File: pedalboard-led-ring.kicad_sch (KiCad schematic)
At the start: 16 parts, among them J1 Conn_02x03, U1 TLC5973, U2 LT3494AEDDBPBF

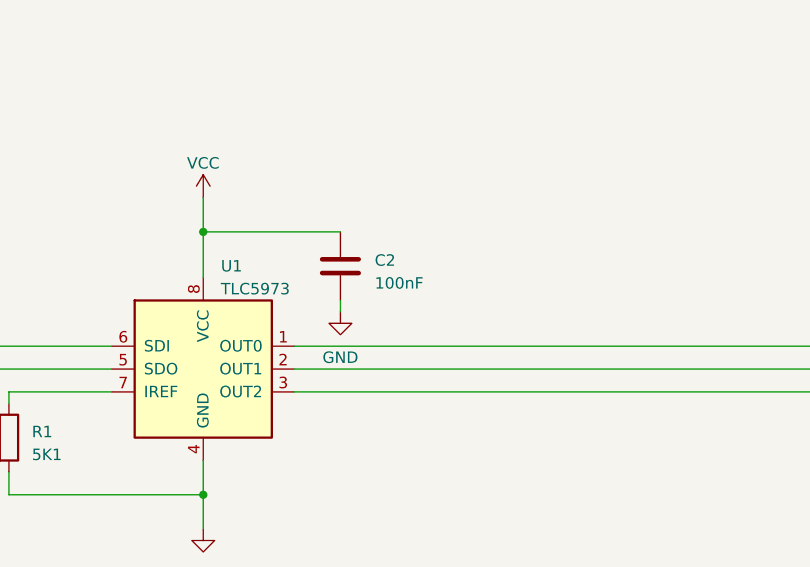
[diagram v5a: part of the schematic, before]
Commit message: Start to collect datasheets and parts on digikey
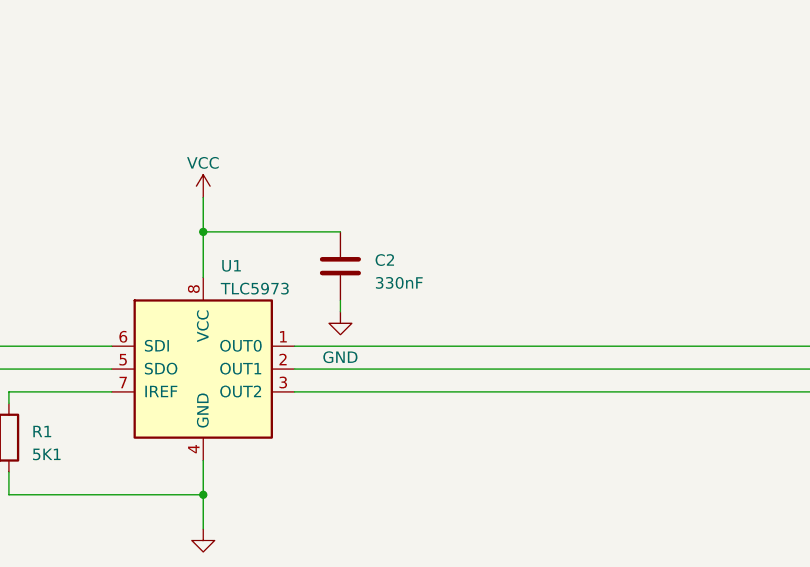
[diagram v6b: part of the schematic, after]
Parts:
- C1, C3, L1: SUPPLIER (none) -> https://www.digikey.ch/de/products/detail/murata-electronic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
- C2: value 100nF -> 330nF; SUPPLIER (none) -> https://www.digikey.ch/de/products/detail/murata-electronic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
- C4: value 0.22uF_0603_25V -> 330nF; SUPPLIER (none) -> https://www.digikey.ch/de/products/detail/murata-electronic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
- D1, D2, D3, D4, D5, D6: SUPPLIER (none) -> https://www.digikey.ch/de/products/detail/harvatek-corporat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
- J1: SUPPLIER (none) -> https://www.digikey.ch/de/products/detail/preci-dip/853-87-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
- R1, R2: SUPPLIER (none) -> https://www.digikey.ch/de/products/detail/samsung-electro-m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
- U1: SUPPLIER (none) -> https://www.digikey.ch/en/products/detail/texas-instruments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
- U2: SUPPLIER Linear Technology -> https://www.digikey.ch/de/products/detail/analog-devices-in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
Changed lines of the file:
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@@
       (effects (font (size 1.27 1.27)) hide)
     )
-    (property "Datasheet" "" (at 210.82 38.1 0)
+    (property "Datasheet" "https://search.murata.co.jp/Ceramy/image/img/A01X/G101/ENG/GRT31CR61H225KE01-01.pdf" (at 210.82 38.1 0)
       (effects (font (size 1.27 1.27)) hide)
     )
@@
       (effects (font (size 1.27 1.27)) hide)
     )
+    (property "SUPPLIER" "https://www.digikey.ch/de/products/detail/murata-electronics/GRT31CR61H225KE01L/5416882" (at 210.82 38.1 0)
+      (effects (font (size 1.27 1.27)) hide)
+    )
     (pin "1")
     (pin "2")
@@
       (effects (font (size 1.27 1.27)) (justify left) hide)
     )
-    (property "Datasheet" "https://search.murata.co.jp/Ceramy/image/img/A01X/G101/ENG/GRM21BR61E106MA73-01.pdf" (at 39.37 40.64 0)
+    (property "Datasheet" "https://search.murata.co.jp/Ceramy/image/img/A01X/G101/ENG/GRT31CR6YA106KE01-01.pdf" (at 39.37 40.64 0)
       (effects (font (size 1.27 1.27)) hide)
     )
@@
       (effects (font (size 1.27 1.27)) hide)
     )
+    (property "SUPPLIER" "https://www.digikey.ch/de/products/detail/murata-electronics/GRT31CR6YA106KE01K/13904946" (at 39.37 40.64 0)
+      (effects (font (size 1.27 1.27)) hide)
+    )
     (pin "1")
     (pin "2")
@@
       (effects (font (size 1.27 1.27)) (justify left) hide)
     )
+    (property "SUPPLIER" "https://www.digikey.ch/de/products/detail/harvatek-corporation/B3803FCH-20C001112U1930/13588742" (at 191.77 77.47 0)
+      (effects (font (size 1.27 1.27)) hide)
+    )
     (pin "1")
     (pin "2")
@@
     (property "Datasheet" "https://media.digikey.com/pdf/Data%20Sheets/Harvatek%20PDFs/B3803FCH-20C001112U1930%20V1.3.pdf" (at 191.77 127 0)
       (effects (font (size 1.27 1.27)) (justify left) hide)
+    )
+    (property "SUPPLIER" "https://www.digikey.ch/de/products/detail/harvatek-corporation/B3803FCH-20C001112U1930/13588742" (at 191.77 123.19 0)
+      (effects (font (size 1.27 1.27)) hide)
     )
     (pin "1")
@@
       (effects (font (size 1.27 1.27)) hide)
     )
+    (property "SUPPLIER" "https://www.digikey.ch/de/products/detail/murata-electronics/LQH32CN150K53L/1016219" (at 57.15 43.18 0)
+      (effects (font (size 1.27 1.27)) hide)
+    )
     (pin "1")
     (pin "2")
@@
       (effects (font (size 1.27 1.27)) hide)
     )
-    (property "Datasheet" "~" (at 91.44 143.51 0)
+    (property "Datasheet" "https://media.digikey.com/pdf/Data%20Sheets/Samsung%20PDFs/RC_Series_ds.pdf" (at 91.44 143.51 0)
+      (effects (font (size 1.27 1.27)) hide)
+    )
+    (property "SUPPLIER" "https://www.digikey.ch/de/products/detail/samsung-electro-mechanics/RC1608F512CS/3965020" (at 91.44 143.51 0)
       (effects (font (size 1.27 1.27)) hide)
     )
@@
       (effects (font (size 1.27 1.27)) (justify left))
     )
-    (property "Value" "0.22uF_0603_25V" (at 52.07 50.8 0)
+    (property "Value" "330nF" (at 52.07 50.8 0)
       (effects (font (size 1.27 1.27)) hide)
     )
@@
       (effects (font (size 1.27 1.27)) (justify left) hide)
     )
-    (property "Datasheet" "" (at 52.07 54.61 0)
+    (property "Datasheet" "https://search.murata.co.jp/Ceramy/image/img/A01X/G101/ENG/GRM216R61A334KA01-01.pdf" (at 52.07 54.61 0)
       (effects (font (size 1.27 1.27)) hide)
     )
@@
       (effects (font (size 1.27 1.27)) (justify left))
     )
+    (property "SUPPLIER" "https://www.digikey.ch/de/products/detail/murata-electronics/GRM216R61A334KA01D/2545090" (at 52.07 54.61 0)
+      (effects (font (size 1.27 1.27)) hide)
+    )
     (pin "1")
     (pin "2")
@@
       (effects (font (size 1.27 1.27)) (justify left) hide)
     )
+    (property "SUPPLIER" "https://www.digikey.ch/de/products/detail/harvatek-corporation/B3803FCH-20C001112U1930/13588742" (at 191.77 92.71 0)
+      (effects (font (size 1.27 1.27)) hide)
+    )
     (pin "1")
     (pin "2")
@@
     (property "Datasheet" "https://media.digikey.com/pdf/Data%20Sheets/Harvatek%20PDFs/B3803FCH-20C001112U1930%20V1.3.pdf" (at 191.77 111.76 0)
       (effects (font (size 1.27 1.27)) (justify left) hide)
+    )
+    (property "SUPPLIER" "https://www.digikey.ch/de/products/detail/harvatek-corporation/B3803FCH-20C001112U1930/13588742" (at 191.77 107.95 0)
+      (effects (font (size 1.27 1.27)) hide)
     )
     (pin "1")
@@
       (effects (font (size 1.27 1.27)) (justify left))
     )
-    (property "Value" "100nF" (at 132.08 126.365 0)
+    (property "Value" "330nF" (at 132.08 126.365 0)
       (effects (font (size 1.27 1.27)) (justify left))
     )
@@
       (effects (font (size 1.27 1.27)) hide)
     )
-    (property "Datasheet" "~" (at 128.27 124.46 0)
+    (property "Datasheet" "https://search.murata.co.jp/Ceramy/image/img/A01X/G101/ENG/GRM216R61A334KA01-01.pdf" (at 128.27 124.46 0)
+      (effects (font (size 1.27 1.27)) hide)
+    )
+    (property "SUPPLIER" "https://www.digikey.ch/de/products/detail/murata-electronics/GRM216R61A334KA01D/2545090" (at 128.27 124.46 0)
       (effects (font (size 1.27 1.27)) hide)
     )
@@
       (effects (font (size 1.27 1.27)) (justify left) hide)
     )
+    (property "SUPPLIER" "https://www.digikey.ch/de/products/detail/harvatek-corporation/B3803FCH-20C001112U1930/13588742" (at 191.77 46.99 0)
+      (effects (font (size 1.27 1.27)) hide)
+    )
     (pin "1")
     (pin "2")
@@
       (effects (font (size 1.27 1.27)) (justify left) hide)
     )
-    (property "Datasheet" "http://www.ti.com/lit/ds/symlink/tlc5973.pdf" (at 105.41 127 0)
+    (property "Datasheet" "https://www.ti.com/lit/ds/symlink/tlc5973.pdf" (at 105.41 127 0)
+      (effects (font (size 1.27 1.27)) hide)
+    )
+    (property "SUPPLIER" "https://www.digikey.ch/en/products/detail/texas-instruments/TLC5973DR/4251271" (at 113.03 135.89 0)
       (effects (font (size 1.27 1.27)) hide)
     )
@@
       (effects (font (size 1.27 1.27)) hide)
     )
-    (property "Datasheet" "~" (at 60.96 30.48 0)
+    (property "Datasheet" "https://media.digikey.com/pdf/Data%20Sheets/Samsung%20PDFs/RC_Series_ds.pdf" (at 60.96 30.48 0)
+      (effects (font (size 1.27 1.27)) hide)
+    )
+    (property "SUPPLIER" "https://www.digikey.ch/de/products/detail/samsung-electro-mechanics/RC1608F3484CS/3965270" (at 60.96 30.48 0)
       (effects (font (size 1.27 1.27)) hide)
     )
@@
       (effects (font (size 1.27 1.27)) (justify left) hide)
     )
+    (property "SUPPLIER" "https://www.digikey.ch/de/products/detail/harvatek-corporation/B3803FCH-20C001112U1930/13588742" (at 191.77 62.23 0)
+      (effects (font (size 1.27 1.27)) hide)
+    )
     (pin "1")
     (pin "2")
@@
       (effects (font (size 1.27 1.27)) hide)
     )
-    (property "Datasheet" "~" (at 54.61 138.43 0)
+    (property "Datasheet" "https://www.precidip.com/AppHost/9696,1/Scripts/Modules/Catalog/Default.aspx?c=7&i=349&p=124&pdf=1&dsku=853-PP-NNN-30-001101" (at 54.61 138.43 0)
+      (effects (font (size 1.27 1.27)) hide)
+    )
+    (property "SUPPLIER" "https://www.digikey.ch/de/products/detail/preci-dip/853-87-006-30-001101/4137372" (at 54.61 138.43 0)
       (effects (font (size 1.27 1.27)) hide)
     )
@@
       (effects (font (size 1.27 1.27)) (justify bottom) hide)
     )
-    (property "Datasheet" "" (at 87.63 44.45 0)
+    (property "Datasheet" "https://www.analog.com/media/en/technical-documentation/data-sheets/3494fb.pdf" (at 87.63 44.45 0)
       (effects (font (size 1.27 1.27)) hide)
     )
@@
       (effects (font (size 1.27 1.27)) (justify bottom) hide)
     )
-    (property "SUPPLIER" "Linear Technology" (at 87.63 44.45 0)
+    (property "SUPPLIER" "https://www.digikey.ch/de/products/detail/analog-devices-inc/LT3494AEDDB-TRPBF/1767840" (at 87.63 44.45 0)
       (effects (font (size 1.27 1.27)) (justify bottom) hide)
     )

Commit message: Fix connector
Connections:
- net GND: now also J1.3 (VCC); no longer J1.4 (VCC)
- net VCC: now also J1.5 (GND); no longer J1.6 (GND)
- net VDC: now also J1.1 (SDO); no longer J1.2 (SDO)
- net at C3.1, L1.2, U2.3 (VCC)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: now also J1.2 (SDI); no longer J1.1 (SDI)
- net at U1.5 (SDO): now also J1.4 (VLED); no longer J1.3 (VLED)
- net at U1.6 (SDI): now also J1.6 (GND); no longer J1.5 (GND)
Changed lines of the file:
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@@
       (effects (font (size 1.27 1.27)) hide)
     )
-    (property "Datasheet" "https://www.precidip.com/AppHost/9696,1/Scripts/Modules/Catalog/Default.aspx?c=7&i=349&p=124&pdf=1&dsku=853-PP-NNN-30-001101" (at 54.61 138.43 0)
+    (property "Datasheet" "~" (at 54.61 138.43 0)
       (effects (font (size 1.27 1.27)) hide)
     )

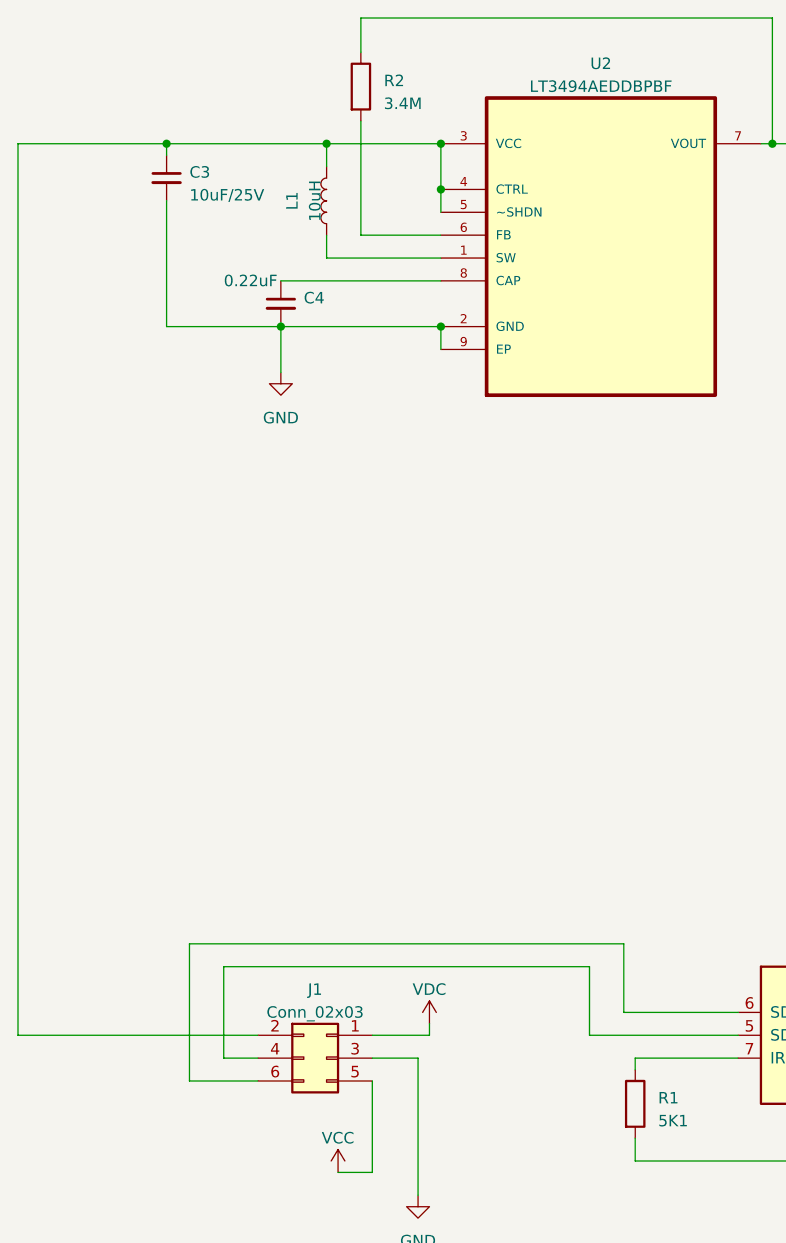
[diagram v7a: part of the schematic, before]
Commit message: Improve copper ground layers
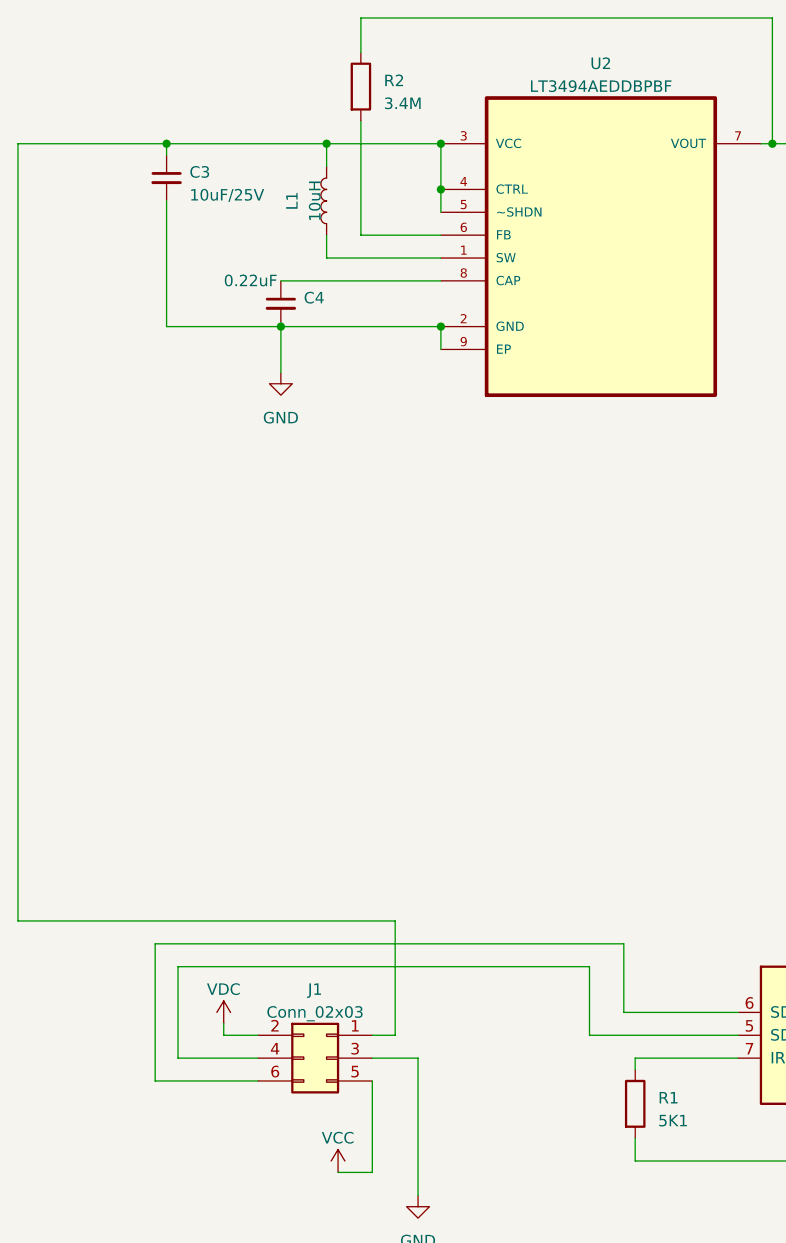
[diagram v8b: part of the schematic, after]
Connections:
- net VDC: now also J1.2 (SDI); no longer J1.1 (SDO)
- net at C3.1, L1.2, U2.3 (VCC)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: now also J1.1 (SDO); no longer J1.2 (SDI)
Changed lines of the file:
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@@
+    (stroke (width 0) (type default))
+  )
+  (wire (pts (xy 22.86 123.19) (xy 64.77 123.19))
     (stroke (width 0) (type default))
   )
@@
     (stroke (width 0) (type default))
   )
-  (wire (pts (xy 49.53 135.89) (xy 22.86 135.89))
-    (stroke (width 0) (type default))
-  )
   (wire (pts (xy 194.31 138.43) (xy 194.31 130.81))
     (stroke (width 0) (type default))
@@
     (stroke (width 0) (type default))
   )
-  (wire (pts (xy 62.23 135.89) (xy 68.58 135.89))
-    (stroke (width 0) (type default))
-  )
-  (wire (pts (xy 41.91 125.73) (xy 41.91 140.97))
+  (wire (pts (xy 64.77 135.89) (xy 62.23 135.89))
+    (stroke (width 0) (type default))
+  )
+  (wire (pts (xy 38.1 125.73) (xy 38.1 140.97))
     (stroke (width 0) (type default))
   )
@@
     (stroke (width 0) (type default))
   )
-  (wire (pts (xy 41.91 140.97) (xy 49.53 140.97))
-    (stroke (width 0) (type default))
-  )
-  (wire (pts (xy 68.58 135.89) (xy 68.58 134.62))
+  (wire (pts (xy 38.1 140.97) (xy 49.53 140.97))
     (stroke (width 0) (type default))
   )
@@
     (stroke (width 0) (type default))
   )
-  (wire (pts (xy 45.72 128.27) (xy 45.72 138.43))
+  (wire (pts (xy 40.64 128.27) (xy 40.64 138.43))
     (stroke (width 0) (type default))
   )
@@
     (stroke (width 0) (type default))
   )
+  (wire (pts (xy 64.77 123.19) (xy 64.77 135.89))
+    (stroke (width 0) (type default))
+  )
   (wire (pts (xy 194.31 35.56) (xy 210.82 35.56))
     (stroke (width 0) (type default))
@@
     (stroke (width 0) (type default))
   )
+  (wire (pts (xy 49.53 135.89) (xy 45.72 135.89))
+    (stroke (width 0) (type default))
+  )
   (wire (pts (xy 113.03 149.86) (xy 113.03 153.67))
     (stroke (width 0) (type default))
@@
     (stroke (width 0) (type default))
   )
-  (wire (pts (xy 90.17 125.73) (xy 41.91 125.73))
+  (wire (pts (xy 90.17 125.73) (xy 38.1 125.73))
+    (stroke (width 0) (type default))
+  )
+  (wire (pts (xy 45.72 135.89) (xy 45.72 134.62))
     (stroke (width 0) (type default))
   )
@@
     (stroke (width 0) (type default))
   )
-  (wire (pts (xy 22.86 36.83) (xy 22.86 135.89))
+  (wire (pts (xy 22.86 36.83) (xy 22.86 123.19))
     (stroke (width 0) (type default))
   )
@@
     (stroke (width 0) (type default))
   )
-  (wire (pts (xy 45.72 138.43) (xy 49.53 138.43))
-    (stroke (width 0) (type default))
-  )
-  (wire (pts (xy 45.72 128.27) (xy 86.36 128.27))
+  (wire (pts (xy 40.64 138.43) (xy 49.53 138.43))
+    (stroke (width 0) (type default))
+  )
+  (wire (pts (xy 40.64 128.27) (xy 86.36 128.27))
     (stroke (width 0) (type default))
   )
@@
     (stroke (width 0) (type default))
   )
-  (symbol (lib_id "power:VDC") (at 68.58 134.62 0) (mirror y) (unit 1)
+  (symbol (lib_id "power:VDC") (at 45.72 134.62 0) (mirror y) (unit 1)
     (in_bom yes) (on_board yes) (dnp no)
-    (property "Reference" "#PWR05" (at 68.58 137.16 0)
+    (property "Reference" "#PWR05" (at 45.72 137.16 0)
       (effects (font (size 1.27 1.27)) hide)
     )
-    (property "Value" "VDC" (at 68.58 130.81 0)
+    (property "Value" "VDC" (at 45.72 130.81 0)
       (effects (font (size 1.27 1.27)))
     )
-    (property "Footprint" "" (at 68.58 134.62 0)
+    (property "Footprint" "" (at 45.72 134.62 0)
       (effects (font (size 1.27 1.27)) hide)
     )
-    (property "Datasheet" "" (at 68.58 134.62 0)
+    (property "Datasheet" "" (at 45.72 134.62 0)
       (effects (font (size 1.27 1.27)) hide)
     )
